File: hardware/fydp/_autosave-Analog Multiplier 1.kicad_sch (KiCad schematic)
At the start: 23 parts, among them J8 Conn_01x02_Pin, U1 LTC2630ISC6-LZ8-TRMPBF, U4 LTC2630ISC6-LZ8-TRMPBF, U5 SN74LVC1G3157DCKR, U6 AD633ARZ-R7

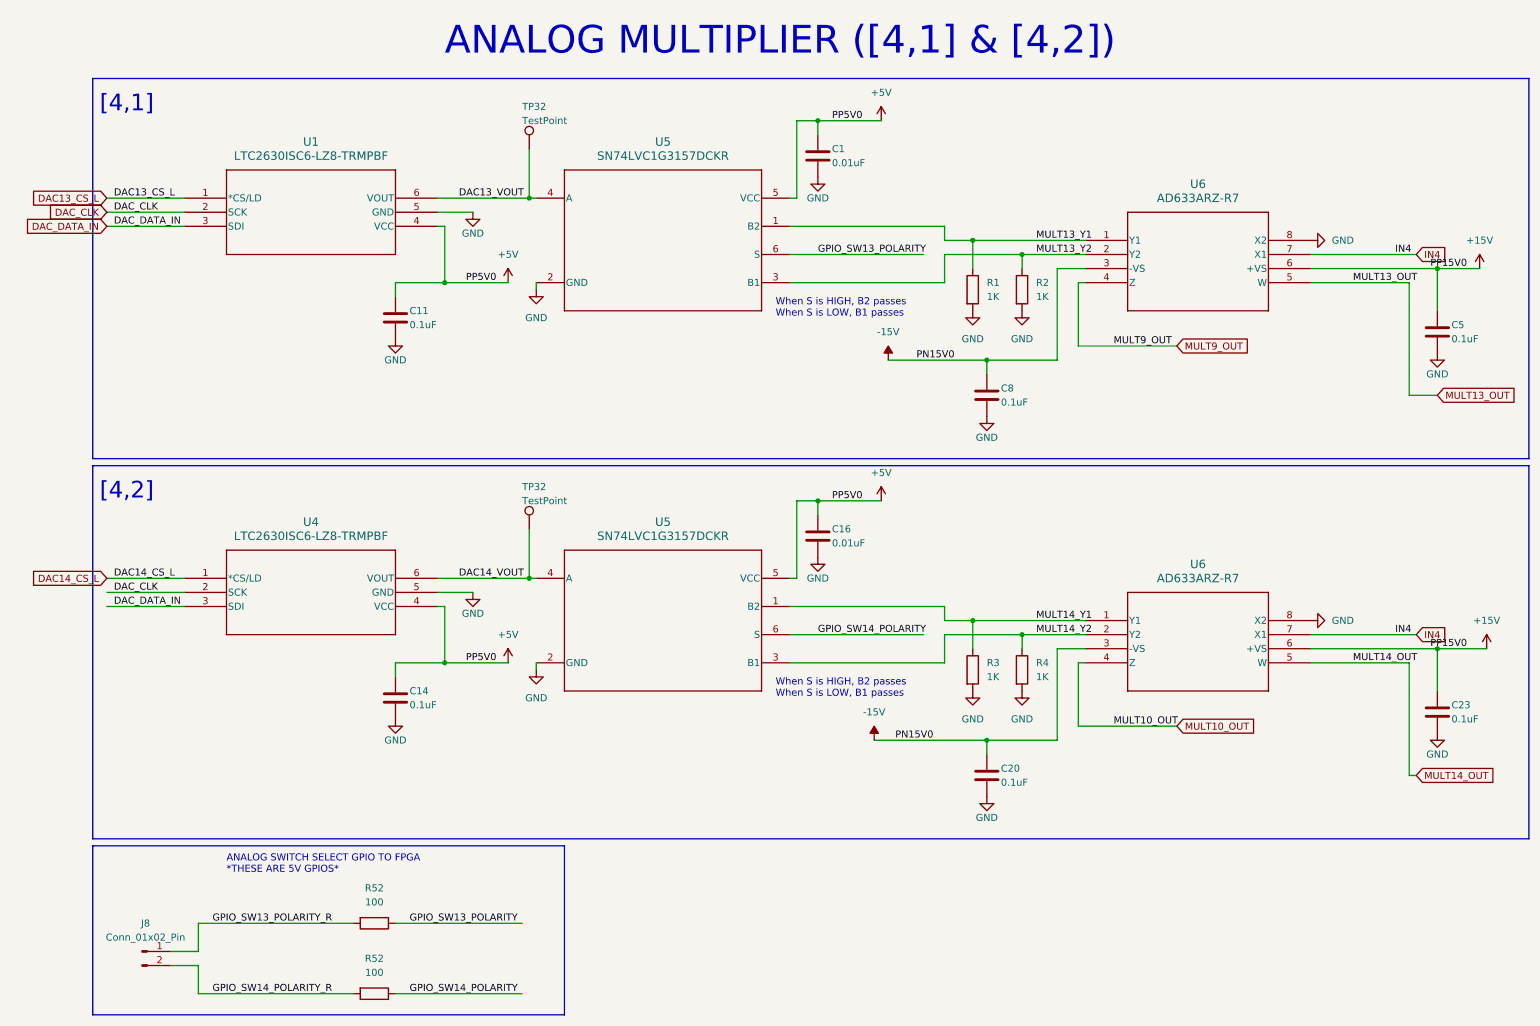
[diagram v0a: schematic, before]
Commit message: Initial layout mostly complete, need to complete lots of routing
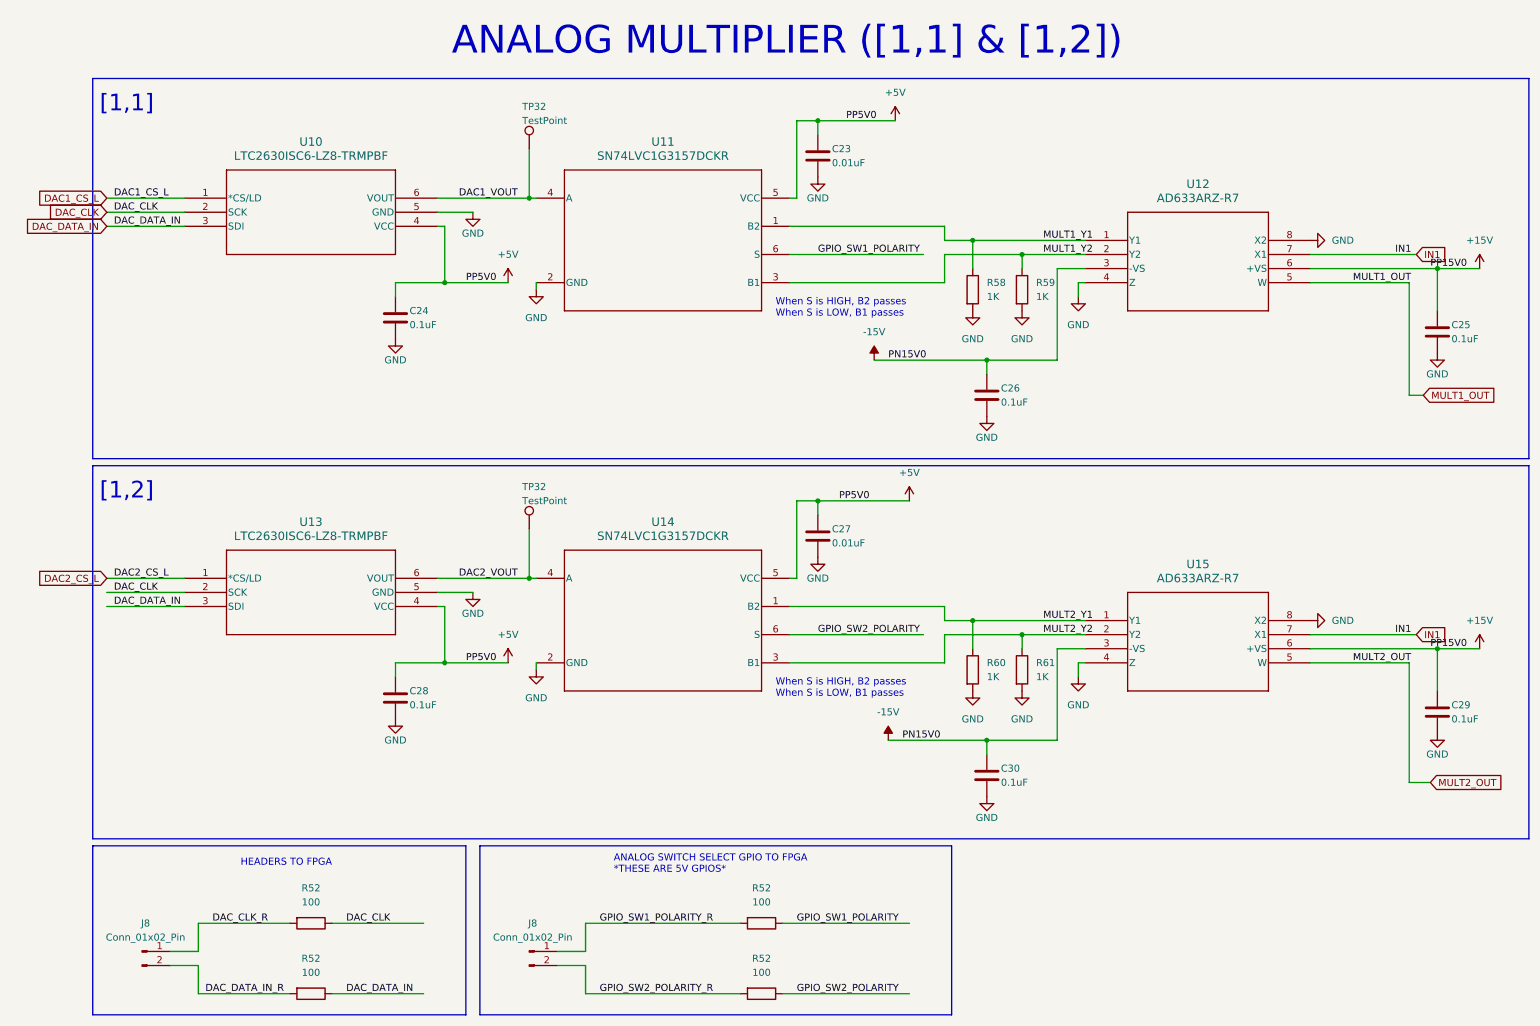
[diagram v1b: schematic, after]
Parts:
- removed C1, C16: 0.01uF, Capacitor_SMD:C_0805_2012Metric, symbol Device:C
- removed C11, C14, C20, C5, C8: 0.1uF, Capacitor_SMD:C_0805_2012Metric, symbol Device:C
- removed J8: Conn_01x02_Pin, Connector_PinHeader_2.54mm:PinHeader_1x02_P2.54mm_Vertical, symbol Connector:Conn_01x02_Pin
- removed R1, R2, R3, R4: 1K, Resistor_SMD:R_0805_2012Metric, symbol Device:R
- removed R52 (x2): 100, Resistor_SMD:R_0805_2012Metric, symbol Device:R
- removed TP32 (x2): TestPoint, TestPoint:TestPoint_Pad_1.0x1.0mm, symbol Connector:TestPoint
- removed U1, U4: LTC2630ISC6-LZ8-TRMPBF, Package_TO_SOT_SMD:SOT-363_SC-70-6_Handsoldering, symbol LTC2630ISC6-LZ8#TRMPBF:LTC2630ISC6-LZ8-TRMPBF
- removed U5 (x2): SN74LVC1G3157DCKR, Package_TO_SOT_SMD:SOT-23-6_Handsoldering, symbol SN74LVC1G3157DCKR:SN74LVC1G3157DCKR
- removed U6 (x2): AD633ARZ-R7, fydp:R_8_ADI, symbol AD633ARZ-R7:AD633ARZ-R7
- added C24, C25, C26, C28, C29, C30: 0.1uF, Capacitor_SMD:C_0805_2012Metric, symbol Device:C
- added C27: 0.01uF, Capacitor_SMD:C_0805_2012Metric, symbol Device:C
- added J8 (x2): Conn_01x02_Pin, Connector_PinHeader_2.54mm:PinHeader_1x02_P2.54mm_Vertical, symbol Connector:Conn_01x02_Pin
- added R52 (x4): 100, Resistor_SMD:R_0805_2012Metric, symbol Device:R
- added R58, R59, R60, R61: 1K, Resistor_SMD:R_0805_2012Metric, symbol Device:R
- added TP32 (x2): TestPoint, TestPoint:TestPoint_Pad_1.0x1.0mm, symbol Connector:TestPoint
- added U10, U13: LTC2630ISC6-LZ8-TRMPBF, Package_TO_SOT_SMD:SOT-363_SC-70-6_Handsoldering, symbol LTC2630ISC6-LZ8#TRMPBF:LTC2630ISC6-LZ8-TRMPBF
- added U11, U14: SN74LVC1G3157DCKR, Package_TO_SOT_SMD:SOT-23-6_Handsoldering, symbol SN74LVC1G3157DCKR:SN74LVC1G3157DCKR
- added U12, U15: AD633ARZ-R7, fydp:R_8_ADI, symbol AD633ARZ-R7:AD633ARZ-R7
- C23: value 0.1uF -> 0.01uF
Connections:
- net +15V: now also C25.1, C29.1, U12.6 (+VS), U15.6 (+VS); no longer C23.1
- net +5V: now also C23.1, C24.1, C27.1, C28.1, U10.4 (VCC), U11.5 (VCC), U13.4 (VCC), U14.5 (VCC)
- net -15V: now also C26.1, C30.1, U12.3 (-VS), U15.3 (-VS)
- net DAC_CLK: now also R52.1, U10.2 (SCK), U13.2 (SCK)
- net DAC_DATA_IN: now also R52.1, U10.3 (SDI), U13.3 (SDI)
- net GND: now also C24.2, C25.2, C26.2, C27.2, C28.2, C29.2, C30.2, R58.2, R59.2, R60.2, R61.2, U10.5 (GND), U11.2 (GND), U12.4 (Z), U12.8 (X2), U13.5 (GND), U14.2 (GND), U15.4 (Z), U15.8 (X2)
- new net DAC1_CS_L: U10.1 (*CS/LD)
- new net DAC1_VOUT: TP32.1, U10.6 (VOUT), U11.4 (A)
- new net DAC2_CS_L: U13.1 (*CS/LD)
- new net DAC2_VOUT: TP32.1, U13.6 (VOUT), U14.4 (A)
- new net DAC_CLK_R: J8.1 (Pin_1), R52.2
- new net DAC_DATA_IN_R: J8.2 (Pin_2), R52.2
- new net GPIO_SW1_POLARITY: R52.1, U11.6 (S)
- new net GPIO_SW1_POLARITY_R: J8.1 (Pin_1), R52.2
- new net GPIO_SW2_POLARITY: R52.1, U14.6 (S)
- new net GPIO_SW2_POLARITY_R: J8.2 (Pin_2), R52.2
- new net IN1: U12.7 (X1), U15.7 (X1)
- new net MULT1_OUT: U12.5 (W)
- new net MULT1_Y1: R58.1, U11.1 (B2), U12.1 (Y1)
- new net MULT1_Y2: R59.1, U11.3 (B1), U12.2 (Y2)
- new net MULT2_OUT: U15.5 (W)
- new net MULT2_Y1: R60.1, U14.1 (B2), U15.1 (Y1)
- new net MULT2_Y2: R61.1, U14.3 (B1), U15.2 (Y2)
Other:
- note added: "ANALOG MULTIPLIER ([1,1] & [1,2])"
- note added: "HEADERS TO FPGA"
- note added: "[1,1]"
- note added: "[1,2]"
- note removed: "ANALOG MULTIPLIER ([4,1] & [4,2])"
- note removed: "[4,1]"
- note removed: "[4,2]"
